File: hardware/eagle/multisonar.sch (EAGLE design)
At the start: 21 parts, among them IC1 ATMEGA328-20P, J1 ARDUINO_R3_SHIELD, Y1 16MHZ

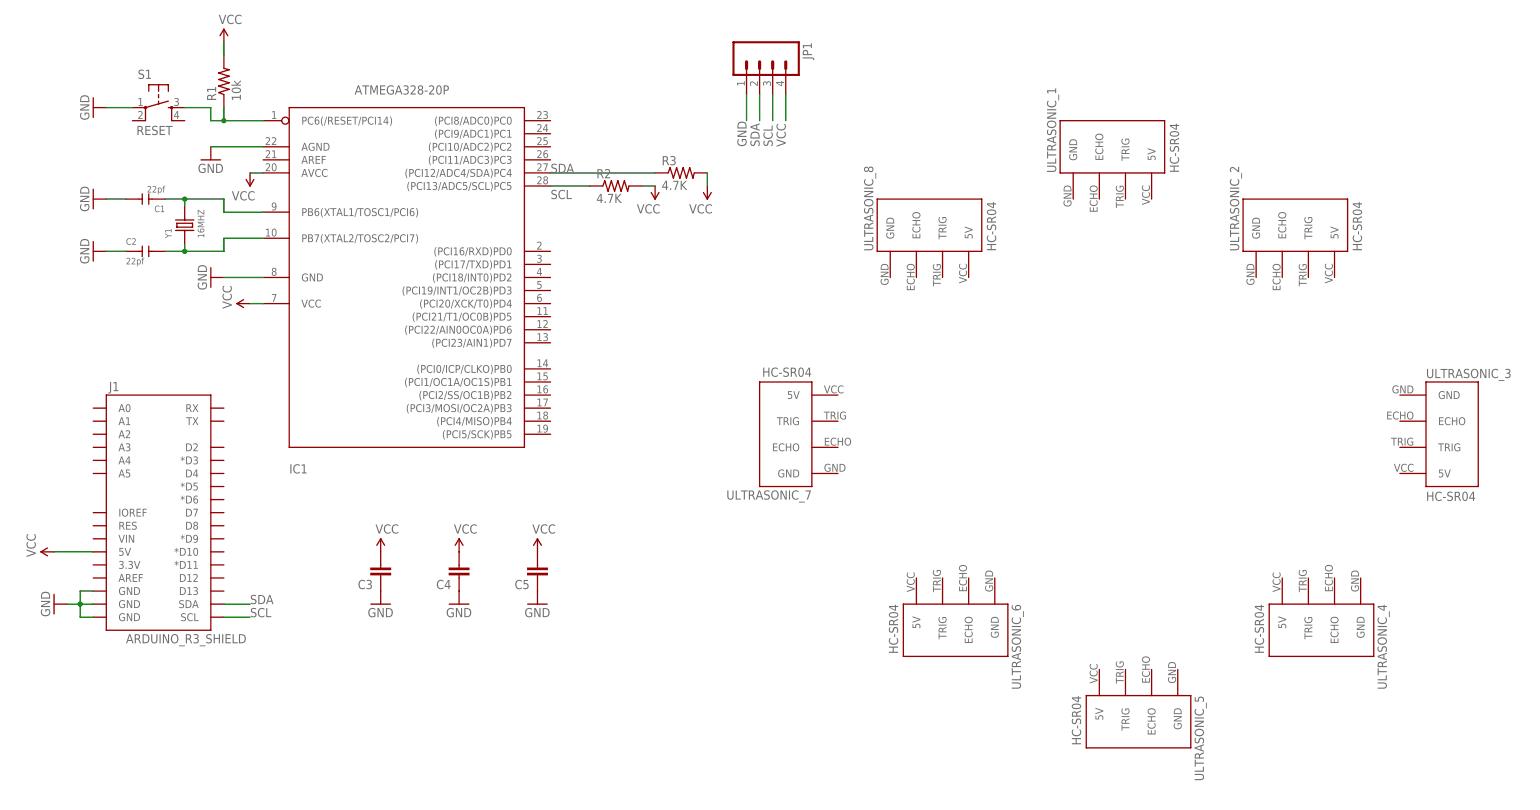
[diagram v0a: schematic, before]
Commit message: Routed power lines
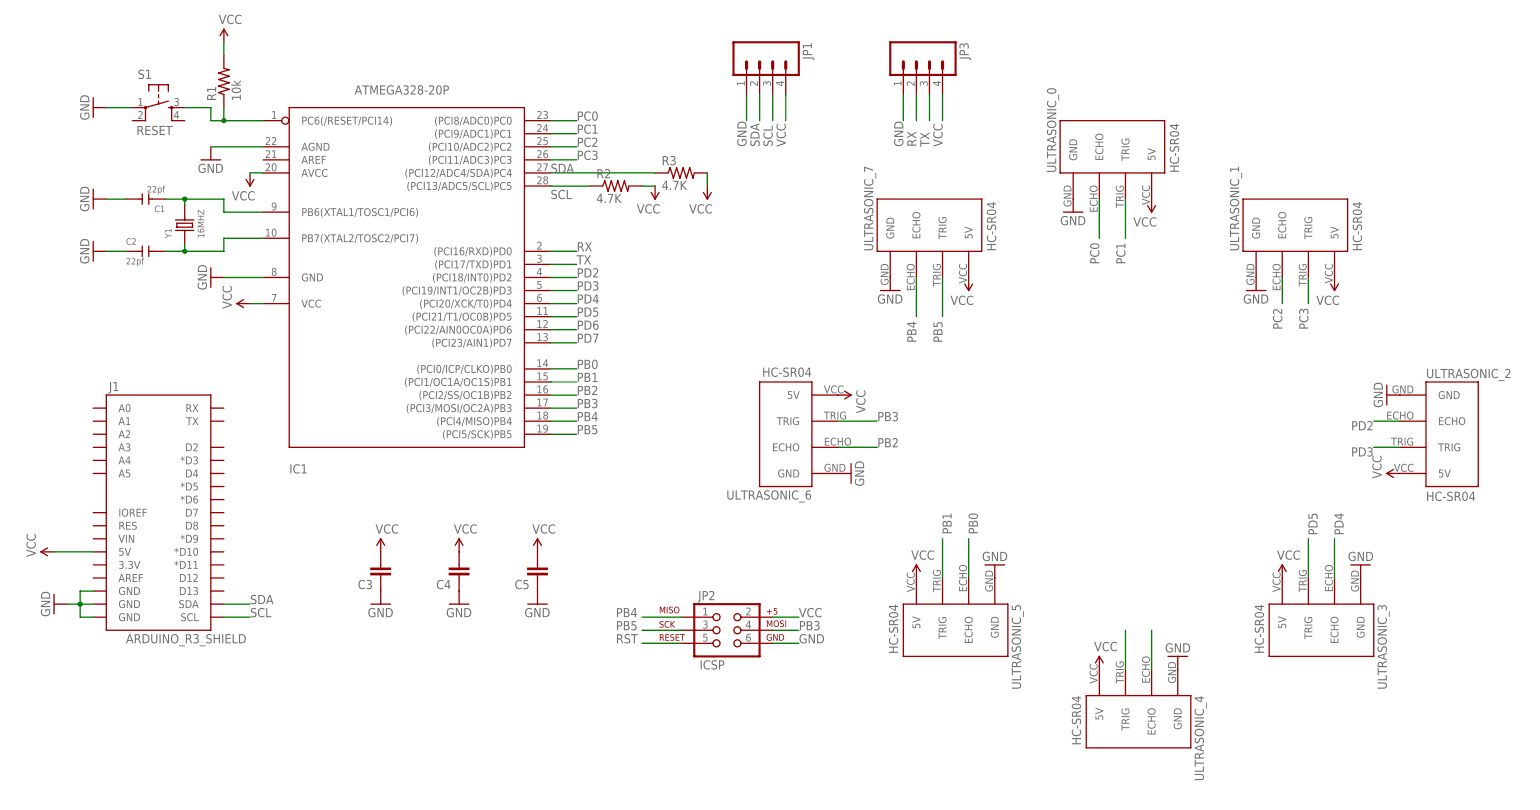
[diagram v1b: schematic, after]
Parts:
- removed ULTRASONIC_8: HC-SR04, Ultrasonic Sensor HC-SR04:HC-SR04
- added JP2: ICSP, SparkFun-Connectors:AVR_SPI_PRG_62X3_LOCK
- added JP3: (no value), SparkFun-Connectors:M04PTH
- added ULTRASONIC_0: HC-SR04, Ultrasonic Sensor HC-SR04:HC-SR04
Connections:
- removed net N$1: IC1.PC6(/RESET/PCI14), R1.1, S1.3
- new net PB0: IC1.(PCI0/ICP/CLKO)PB0, ULTRASONIC_5.ECHO
- new net PB1: IC1.(PCI1/OC1A/OC1S)PB1, ULTRASONIC_5.TRIG
- new net PB2: IC1.(PCI2/SS/OC1B)PB2, ULTRASONIC_6.ECHO
- new net PB3: IC1.(PCI3/MOSI/OC2A)PB3, JP2.4, ULTRASONIC_6.TRIG
- new net PB4: IC1.(PCI4/MISO)PB4, JP2.1, ULTRASONIC_7.ECHO
- new net PB5: IC1.(PCI5/SCK)PB5, JP2.3, ULTRASONIC_7.TRIG
- new net PC0: IC1.(PCI8/ADC0)PC0, ULTRASONIC_0.ECHO
- new net PC1: IC1.(PCI9/ADC1)PC1, ULTRASONIC_0.TRIG
- new net PC2: IC1.(PCI10/ADC2)PC2, ULTRASONIC_1.ECHO
- new net PC3: IC1.(PCI11/ADC3)PC3, ULTRASONIC_1.TRIG
- new net PD2: IC1.(PCI18/INT0)PD2, ULTRASONIC_2.ECHO
- new net PD3: IC1.(PCI19/INT1/OC2B)PD3, ULTRASONIC_2.TRIG
- new net PD4: IC1.(PCI20/XCK/T0)PD4, ULTRASONIC_3.ECHO
- new net PD5: IC1.(PCI21/T1/OC0B)PD5, ULTRASONIC_3.TRIG
- new net PD6: IC1.(PCI22/AIN0OC0A)PD6, ULTRASONIC_4.ECHO
- new net PD7: IC1.(PCI23/AIN1)PD7, ULTRASONIC_4.TRIG
- new net RST: IC1.PC6(/RESET/PCI14), JP2.5, R1.1, S1.3
- new net RX: IC1.(PCI16/RXD)PD0, JP3.2
- new net TX: IC1.(PCI17/TXD)PD1, JP3.3
- net GND: now also JP2.6, JP3.1, ULTRASONIC_0.GND, ULTRASONIC_1.GND, ULTRASONIC_2.GND, ULTRASONIC_3.GND, ULTRASONIC_4.GND, ULTRASONIC_5.GND, ULTRASONIC_6.GND, ULTRASONIC_7.GND
- net VCC: now also JP2.2, JP3.4, ULTRASONIC_0.5V, ULTRASONIC_1.5V, ULTRASONIC_2.5V, ULTRASONIC_3.5V, ULTRASONIC_4.5V, ULTRASONIC_5.5V, ULTRASONIC_6.5V, ULTRASONIC_7.5V
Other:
- moved on the sheet: ULTRASONIC_1, ULTRASONIC_2, ULTRASONIC_3, ULTRASONIC_4, ULTRASONIC_5, ULTRASONIC_6, ULTRASONIC_7

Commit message: Routed all components
TO-DO: Add silk screen
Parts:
- removed JP1: (no value), SparkFun-Connectors:M04PTH
- added D1: (no value), Seeed-OPL-Diode:DIODE'1206'
- added I2C: 5p-2.54, Seeed-OPL-Connector:DIP-BLACK-FEMALE-HEADER-VERT(5P-2.54)
- added R5: 220, SparkFun-Resistors:RESISTOR1206
- R1: value 10k -> 4.7K
- renumbered JP3 to UART
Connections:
- removed net RX: IC1.(PCI16/RXD)PD0, UART.2
- removed net TX: IC1.(PCI17/TXD)PD1, UART.3
- new net N$1: R1.1, S1.4
- new net N$2: D1.-, R5.1
- new net RX/IRQ: I2C.2, IC1.(PCI16/RXD)PD0, UART.2
- new net TX/LED: D1.+, IC1.(PCI17/TXD)PD1, UART.3
- net GND: now also I2C.1, R5.2, S1.2; no longer JP1.1
- net PB0: now also ULTRASONIC_4.TRIG; no longer ULTRASONIC_5.ECHO
- net PB1: now also ULTRASONIC_4.ECHO; no longer ULTRASONIC_5.TRIG
- net PB2: now also ULTRASONIC_3.ECHO; no longer ULTRASONIC_6.ECHO
- net PB3: now also ULTRASONIC_3.TRIG; no longer ULTRASONIC_6.TRIG
- net PB4: now also ULTRASONIC_2.ECHO; no longer ULTRASONIC_7.ECHO
- net PB5: now also ULTRASONIC_2.TRIG; no longer ULTRASONIC_7.TRIG
- net PC0: now also ULTRASONIC_1.ECHO; no longer ULTRASONIC_0.ECHO
- net PC1: now also ULTRASONIC_1.TRIG; no longer ULTRASONIC_0.TRIG
- net PC2: now also ULTRASONIC_0.ECHO; no longer ULTRASONIC_1.ECHO
- net PC3: now also ULTRASONIC_0.TRIG; no longer ULTRASONIC_1.TRIG
- net PD2: now also ULTRASONIC_7.ECHO; no longer ULTRASONIC_2.ECHO
- net PD3: now also ULTRASONIC_7.TRIG; no longer ULTRASONIC_2.TRIG
- net PD4: now also ULTRASONIC_6.TRIG; no longer ULTRASONIC_3.ECHO
- net PD5: now also ULTRASONIC_6.ECHO; no longer ULTRASONIC_3.TRIG
- net PD6: now also ULTRASONIC_5.ECHO; no longer ULTRASONIC_4.ECHO
- net PD7: now also ULTRASONIC_5.TRIG; no longer ULTRASONIC_4.TRIG
- net RST: no longer R1.1
- net SCL: now also I2C.4; no longer JP1.3
- net SDA: now also I2C.3; no longer JP1.2
- net VCC: now also I2C.5; no longer JP1.4
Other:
- moved on the sheet: R1, S1

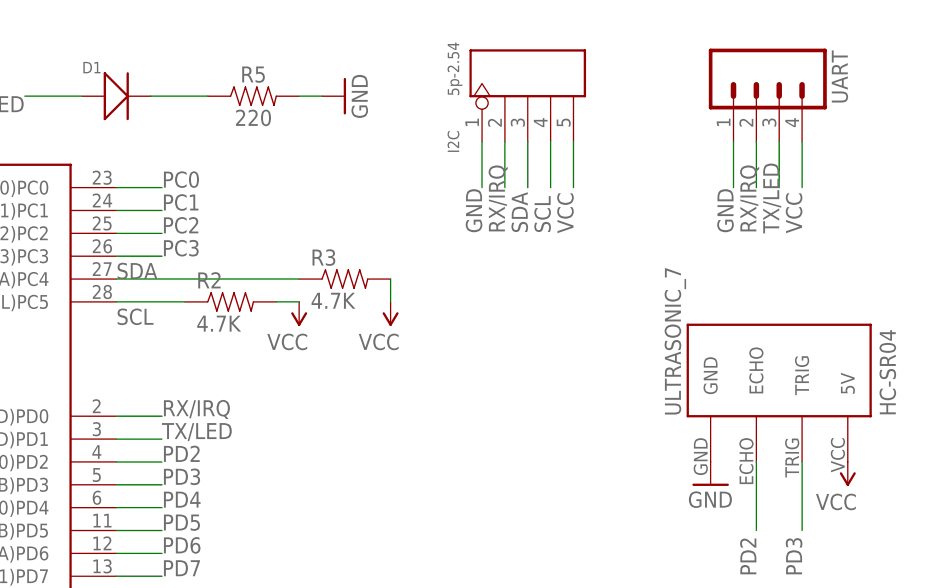
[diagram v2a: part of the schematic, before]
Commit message: Change IRQ to INT for clarity
It should be easier to explain to novice users
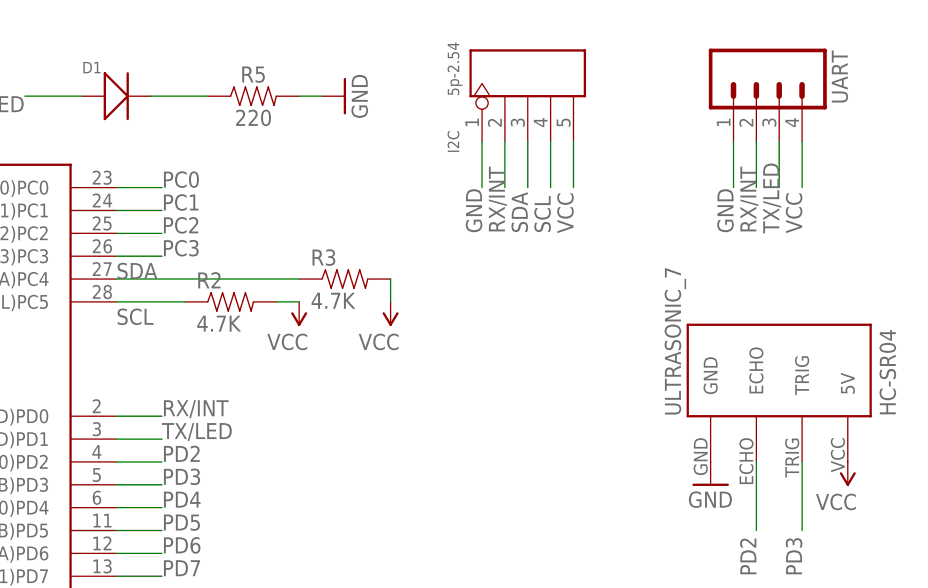
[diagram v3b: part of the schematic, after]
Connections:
- net RX/IRQ renamed RX/INT
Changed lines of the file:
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@@
 </segment>
 </net>
-<net name="RX/IRQ" class="0">
+<net name="RX/INT" class="0">
 <segment>
 <pinref part="UART" gate="G$1" pin="2"/>

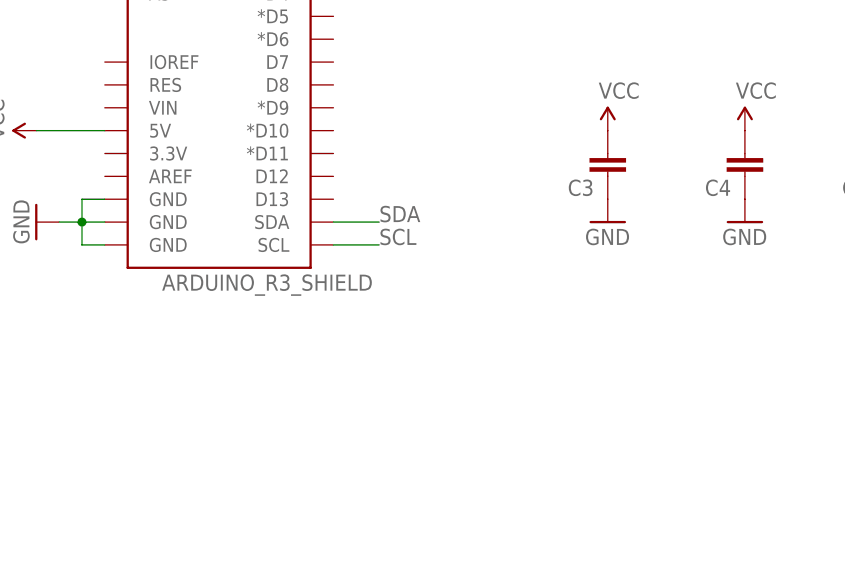
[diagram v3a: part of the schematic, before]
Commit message: Use the lock package for easier soldering
The lock arduino shield package is used to facilitate
the headers staying in place while soldering
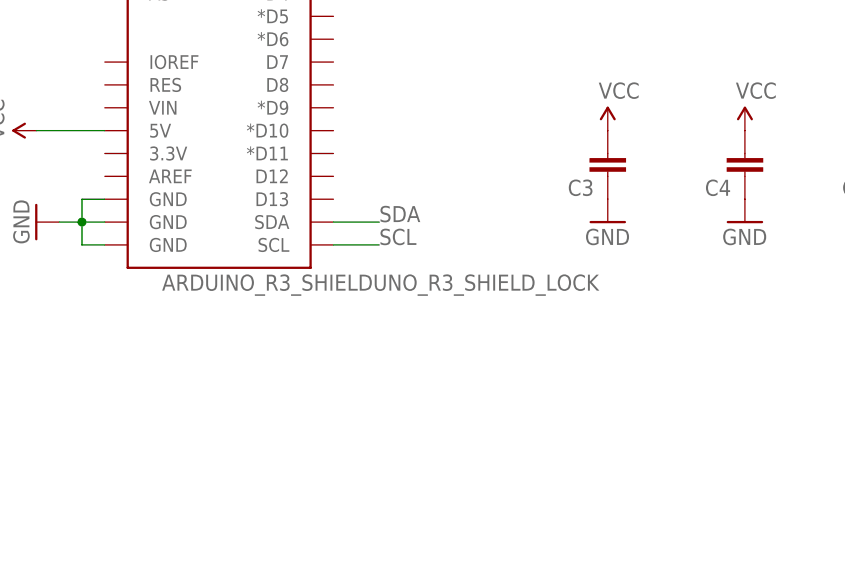
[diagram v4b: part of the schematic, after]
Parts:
- J1: value ARDUINO_R3_SHIELD -> ARDUINO_R3_SHIELDUNO_R3_SHIELD_LOCK; device SparkFun-Boards:ARDUINO_R3_SHIELD -> SparkFun-Boards:ARDUINO_R3_SHIELDUNO_R3_SHIELD_LOCK
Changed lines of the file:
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@@
 <?xml version="1.0" encoding="utf-8"?>
 <!DOCTYPE eagle SYSTEM "eagle.dtd">
-<eagle version="8.2.2">
+<eagle version="8.3.0">
 <drawing>
 <settings>
 <setting alwaysvectorfont="no"/>
+<setting keepoldvectorfont="yes"/>
 <setting verticaltext="up"/>
 </settings>
 <grid distance="0.1" unitdist="inch" unit="inch" style="lines" multiple="1" display="no" altdistance="0.01" altunitdist="inch" altunit="inch"/>
 <layers>
-<layer number="1" name="Top" color="4" fill="1" visible="no" active="no"/>
-<layer number="2" name="Route2" color="1" fill="3" visible="no" active="no"/>
-<layer number="3" name="Route3" color="4" fill="3" visible="no" active="no"/>
-<layer number="4" name="Route4" color="1" fill="4" visible="no" active="no"/>
-<layer number="5" name="Route5" color="4" fill="4" visible="no" active="no"/>
-<layer number="6" name="Route6" color="1" fill="8" visible="no" active="no"/>
-<layer number="7" name="Route7" color="4" fill="8" visible="no" active="no"/>
-<layer number="8" name="Route8" color="1" fill="2" visible="no" active="no"/>
-<layer number="9" name="Route9" color="4" fill="2" visible="no" active="no"/>
-<layer number="10" name="Route10" color="1" fill="7" visible="no" active="no"/>
-<layer number="11" name="Route11" color="4" fill="7" visible="no" active="no"/>
-<layer number="12" name="Route12" color="1" fill="5" visible="no" active="no"/>
-<layer number="13" name="Route13" color="4" fill="5" visible="no" active="no"/>
-<layer number="14" name="Route14" color="1" fill="6" visible="no" active="no"/>
-<layer number="15" name="Route15" color="4" fill="6" visible="no" active="no"/>
-<layer number="16" name="Bottom" color="1" fill="1" visible="no" active="no"/>
-<layer number="17" name="Pads" color="2" fill="1" visible="no" active="no"/>
-<layer number="18" name="Vias" color="2" fill="1" visible="no" active="no"/>
-<layer number="19" name="Unrouted" color="6" fill="1" visible="no" active="no"/>
-<layer number="20" name="Dimension" color="15" fill="1" visible="no" active="no"/>
-<layer number="21" name="tPlace" color="7" fill="1" visible="no" active="no"/>
-<layer number="22" name="bPlace" color="7" fill="1" visible="no" active="no"/>
-<layer number="23" name="tOrigins" color="15" fill="1" visible="no" active="no"/>
-<layer number="24" name="bOrigins" color="15" fill="1" visible="no" active="no"/>
-<layer number="25" name="tNames" color="7" fill="1" visible="no" active="no"/>
-<layer number="26" name="bNames" color="7" fill="1" visible="no" active="no"/>
-<layer number="27" name="tValues" color="7" fill="1" visible="no" active="no"/>
-<layer number="28" name="bValues" color="7" fill="1" visible="no" active="no"/>
+<layer number="1" name="Top" color="4" fill="1" visible="yes" active="no"/>
+<layer number="2" name="Route2" color="1" fill="3" visible="yes" active="no"/>
+<layer number="3" name="Route3" color="4" fill="3" visible="yes" active="no"/>
+<layer number="4" name="Route4" color="1" fill="4" visible="yes" active="no"/>
+<layer number="5" name="Route5" color="4" fill="4" visible="yes" active="no"/>
+<layer number="6" name="Route6" color="1" fill="8" visible="yes" active="no"/>
+<layer number="7" name="Route7" color="4" fill="8" visible="yes" active="no"/>
+<layer number="8" name="Route8" color="1" fill="2" visible="yes" active="no"/>
+<layer number="9" name="Route9" color="4" fill="2" visible="yes" active="no"/>
+<layer number="10" name="Route10" color="1" fill="7" visible="yes" active="no"/>
+<layer number="11" name="Route11" color="4" fill="7" visible="yes" active="no"/>
+<layer number="12" name="Route12" color="1" fill="5" visible="yes" active="no"/>
+<layer number="13" name="Route13" color="4" fill="5" visible="yes" active="no"/>
+<layer number="14" name="Route14" color="1" fill="6" visible="yes" active="no"/>
+<layer number="15" name="Route15" color="4" fill="6" visible="yes" active="no"/>
+<layer number="16" name="Bottom" color="1" fill="1" visible="yes" active="no"/>
+<layer number="17" name="Pads" color="2" fill="1" visible="yes" active="no"/>
+<layer number="18" name="Vias" color="2" fill="1" visible="yes" active="no"/>
+<layer number="19" name="Unrouted" color="6" fill="1" visible="yes" active="no"/>
+<layer number="20" name="Dimension" color="15" fill="1" visible="yes" active="no"/>
+<layer number="21" name="tPlace" color="7" fill="1" visible="yes" active="no"/>
+<layer number="22" name="bPlace" color="7" fill="1" visible="yes" active="no"/>
+<layer number="23" name="tOrigins" color="15" fill="1" visible="yes" active="no"/>
+<layer number="24" name="bOrigins" color="15" fill="1" visible="yes" active="no"/>
+<layer number="25" name="tNames" color="7" fill="1" visible="yes" active="no"/>
+<layer number="26" name="bNames" color="7" fill="1" visible="yes" active="no"/>
+<layer number="27" name="tValues" color="7" fill="1" visible="yes" active="no"/>
+<layer number="28" name="bValues" color="7" fill="1" visible="yes" active="no"/>
 <layer number="29" name="tStop" color="7" fill="3" visible="no" active="no"/>
 <layer number="30" name="bStop" color="7" fill="6" visible="no" active="no"/>
@@
 <layer number="35" name="tGlue" color="7" fill="4" visible="no" active="no"/>
 <layer number="36" name="bGlue" color="7" fill="5" visible="no" active="no"/>
-<layer number="37" name="tTest" color="7" fill="1" visible="no" active="no"/>
-<layer number="38" name="bTest" color="7" fill="1" visible="no" active="no"/>
+<layer number="37" name="tTest" color="7" fill="1" visible="yes" active="no"/>
+<layer number="38" name="bTest" color="7" fill="1" visible="yes" active="no"/>
 <layer number="39" name="tKeepout" color="4" fill="11" visible="no" active="no"/>
 <layer number="40" name="bKeepout" color="1" fill="11" visible="no" active="no"/>
@@
 <layer number="44" name="Drills" color="7" fill="1" visible="no" active="no"/>
 <layer number="45" name="Holes" color="7" fill="1" visible="no" active="no"/>
-<layer number="46" name="Milling" color="3" fill="1" visible="no" active="no"/>
-<layer number="47" name="Measures" color="7" fill="1" visible="no" active="no"/>
-<layer number="48" name="Document" color="7" fill="1" visible="no" active="no"/>
-<layer number="49" name="Reference" color="7" fill="1" visible="no" active="no"/>
-<layer number="50" name="dxf" color="7" fill="1" visible="no" active="no"/>
-<layer number="51" name="tDocu" color="7" fill="1" visible="no" active="no"/>
-<layer number="52" name="bDocu" color="7" fill="1" visible="no" active="no"/>
-<layer number="53" name="tGND_GNDA" color="7" fill="9" visible="no" active="no"/>
-<layer number="54" name="bGND_GNDA" color="1" fill="9" visible="no" active="no"/>
-<layer number="56" name="wert" color="7" fill="1" visible="no" active="no"/>
-<layer number="57" name="tCAD" color="7" fill="1" visible="no" active="no"/>
-<layer number="59" name="tCarbon" color="7" fill="1" visible="no" active="no"/>
-<layer number="60" name="bCarbon" color="7" fill="1" visible="no" active="no"/>
+<layer number="46" name="Milling" color="3" fill="1" visible="yes" active="no"/>
+<layer number="47" name="Measures" color="7" fill="1" visible="yes" active="no"/>
+<layer number="48" name="Document" color="7" fill="1" visible="yes" active="no"/>
+<layer number="49" name="Reference" color="7" fill="1" visible="yes" active="no"/>
+<layer number="50" name="dxf" color="7" fill="1" visible="yes" active="no"/>
+<layer number="51" name="tDocu" color="7" fill="1" visible="yes" active="no"/>
+<layer number="52" name="bDocu" color="7" fill="1" visible="yes" active="no"/>
+<layer number="53" name="tGND_GNDA" color="7" fill="9" visible="yes" active="no"/>
+<layer number="54" name="bGND_GNDA" color="1" fill="9" visible="yes" active="no"/>
+<layer number="56" name="wert" color="7" fill="1" visible="yes" active="no"/>
+<layer number="57" name="tCAD" color="7" fill="1" visible="yes" active="no"/>
+<layer number="59" name="tCarbon" color="7" fill="1" visible="yes" active="no"/>
+<layer number="60" name="bCarbon" color="7" fill="1" visible="yes" active="no"/>
 <layer number="90" name="Modules" color="5" fill="1" visible="yes" active="yes"/>
 <layer number="91" name="Nets" color="2" fill="1" visible="yes" active="yes"/>
@@
 <part name="SUPPLY7" library="SparkFun-Aesthetics" deviceset="VCC" device=""/>
 <part name="SUPPLY8" library="SparkFun-Aesthetics" deviceset="VCC" device=""/>
-<part name="J1" library="SparkFun-Boards" deviceset="ARDUINO_R3_SHIELD" device=""/>
+<part name="J1" library="SparkFun-Boards" deviceset="ARDUINO_R3_SHIELD" device="UNO_R3_SHIELD_LOCK" value="ARDUINO_R3_SHIELDUNO_R3_SHIELD_LOCK"/>
 <part name="SUPPLY9" library="SparkFun-Aesthetics" deviceset="VCC" device=""/>
 <part name="JP2" library="SparkFun-Connectors" deviceset="AVR_SPI_PRG_6" device="2X3_LOCK" value="ICSP"/>
